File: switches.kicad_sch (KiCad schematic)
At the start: 149 parts, among them SW10 SW_Push, SW11 SW_Push, SW12 SW_Push, SW13 SW_Push, SW14 SW_Push, SW15 SW_Push, SW16 SW_Push, SW17 SW_Push, SW18 SW_Push, SW19 SW_Push, SW20 SW_Push, SW21 SW_Push, SW22 SW_Push, SW23 SW_Push, SW24 SW_Push, SW25 SW_Push, SW26 SW_Push, SW27 SW_Push, SW28 SW_Push, SW29 SW_Push, SW3 SW_Push, SW30 SW_Push, SW31 SW_Push, SW32 SW_Push, SW33 SW_Push, SW34 SW_Push, SW35 SW_Push, SW36 SW_Push, SW37 SW_Push, SW38 SW_Push, SW39 SW_Push, SW4 SW_Push, SW40 SW_Push, SW41 SW_Push, SW42 SW_Push, SW43 SW_Push, SW44 SW_Push, SW45 SW_Push, SW46 SW_Push, SW47 SW_Push, SW48 SW_Push, SW49 SW_Push, SW5 SW_Push, SW50 SW_Push, SW51 SW_Push, SW52 SW_Push, SW53 SW_Push, SW54 SW_Push, SW55 SW_Push, SW56 SW_Push, SW57 SW_Push, SW58 SW_Push, SW59 SW_Push, SW6 SW_Push, SW60 SW_Push, SW61 SW_Push, SW62 SW_Push, SW63 SW_Push, SW64 SW_Push, SW65 SW_Push, SW66 SW_Push, SW67 SW_Push, SW68 SW_Push, SW69 SW_Push, SW7 SW_Push, SW70 SW_Push, SW71 SW_Push, SW72 SW_Push, SW73 SW_Push, SW74 SW_Push, SW75 SW_Push, SW76 SW_Push, SW77 SW_Push, SW78 SW_Push, SW79 SW_Push, SW8 SW_Push, SW80 SW_Push, SW81 SW_Push, SW82 SW_Push, SW83 SW_Push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

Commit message: update footpoint and add pcb layout
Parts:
- SW10, SW11, SW12, SW13, SW14, SW15, SW16, SW17, SW18, SW19, SW20, SW21, SW22, SW23, SW24, SW25, SW26, SW27, SW28, SW29, SW3, SW30, SW31, SW32, SW33, SW34, SW35, SW36, SW37, SW38, SW39, SW4, SW40, SW41, SW42, SW43, SW44, SW45, SW46, SW47, SW48, SW49, SW5, SW50, SW51, SW52, SW53, SW54, SW55, SW56, SW57, SW58, SW59, SW6, SW60, SW61, SW62, SW63, SW64, SW65, SW66, SW67, SW68, SW69, SW7, SW70, SW71, SW72, SW73, SW74, SW75, SW76, SW77, SW78, SW79, SW8, SW80, SW81, SW82, SW83, SW84, SW85, SW86, SW9: footprint keyswitches:Kailh_socket_MX_optional -> keyswitches:Kailh_socket_MX

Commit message: remove key
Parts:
- removed D13, D48: 1N4148, Diode_SMD:D_0603_1608Metric, symbol Diode:1N4148
- removed SW12, SW13, SW17, SW19, SW33, SW34, SW4, SW55, SW57, SW6, SW63, SW64, SW70, SW72, SW77, SW8, SW81, SW83, SW85: SW_Push, keyswitches:Kailh_socket_MX, symbol Switch:SW_Push

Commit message: change pin default and try layout
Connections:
- net col6: no longer SW32.2
- net col7: now also SW32.2

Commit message: modify pcb footprint
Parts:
- D10, D11, D12, D14, D15, D16, D17, D18, D19, D20, D21, D22, D23, D24, D25, D26, D27, D28, D29, D30, D31, D32, D33, D34, D35, D36, D37, D38, D39, D4, D40, D41, D42, D43, D44, D45, D46, D47, D49, D5, D50, D51, D52, D53, D54, D55, D56, D57, D58, D59, D6, D60, D61, D62, D63, D64, D65, D66, D67, D68, D7, D8, D9: value 1N4148 -> (none); footprint Diode_SMD:D_0603_1608Metric -> (none)
- SW10, SW11, SW14, SW15, SW16, SW18, SW20, SW21, SW22, SW23, SW24, SW25, SW26, SW27, SW28, SW29, SW3, SW30, SW31, SW32, SW35, SW36, SW37, SW38, SW39, SW40, SW41, SW42, SW43, SW44, SW45, SW46, SW47, SW48, SW49, SW5, SW50, SW51, SW52, SW53, SW54, SW56, SW58, SW59, SW60, SW61, SW62, SW65, SW66, SW67, SW68, SW69, SW7, SW71, SW73, SW74, SW75, SW76, SW78, SW79, SW80, SW82, SW84, SW86, SW9: value SW_Push -> (none); footprint keyswitches:Kailh_socket_MX -> (none)

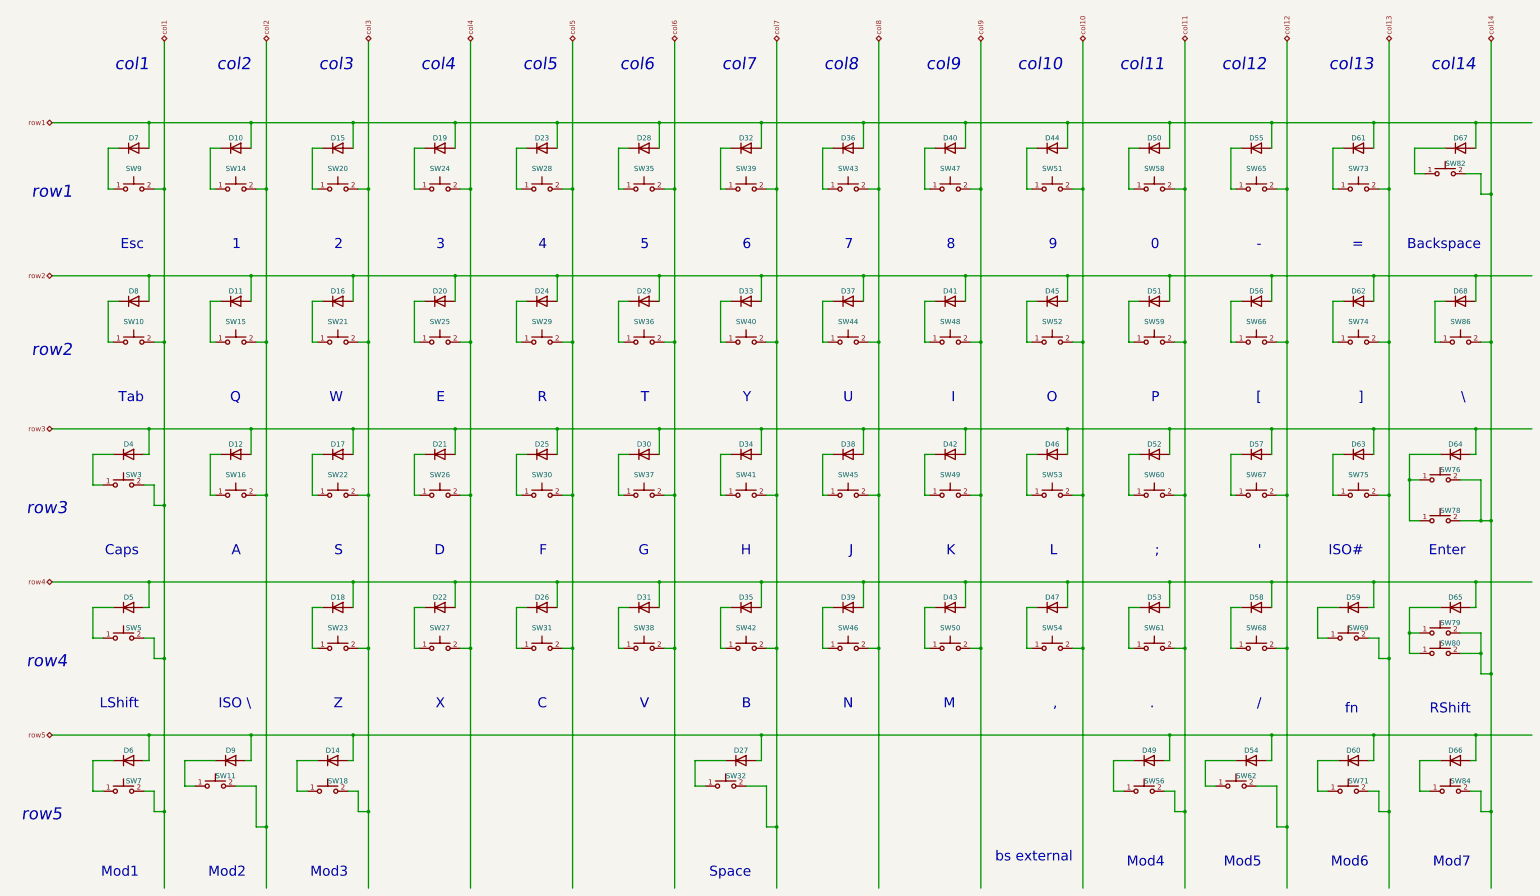
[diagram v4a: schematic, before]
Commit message: change Diode direction and update PR #1 footprint
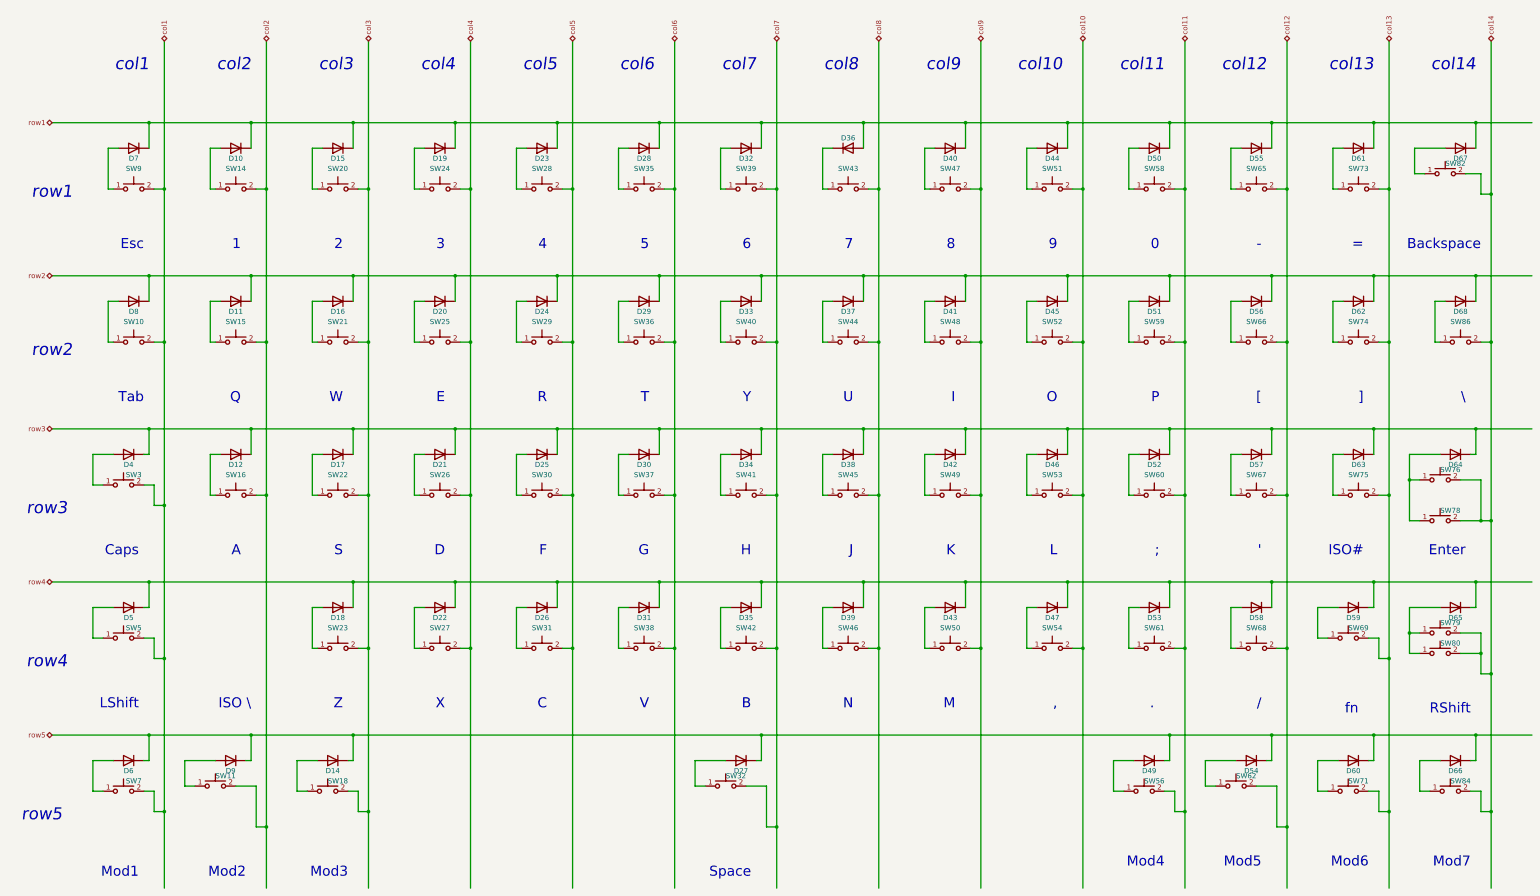
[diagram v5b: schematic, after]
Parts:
- D10, D11, D12, D14, D15, D16, D17, D18, D19, D20, D21, D22, D23, D24, D25, D26, D27, D28, D29, D30, D31, D32, D33, D34, D35, D36, D37, D38, D39, D4, D40, D41, D42, D43, D44, D45, D46, D47, D49, D5, D50, D51, D52, D53, D54, D55, D56, D57, D58, D59, D6, D60, D61, D62, D63, D64, D65, D66, D67, D68, D7, D8, D9: value (none) -> 1N4148; footprint (none) -> Diode_SMD:D_0805_2012Metric
- SW10, SW11, SW14, SW15, SW16, SW18, SW20, SW21, SW22, SW23, SW24, SW25, SW26, SW27, SW28, SW29, SW3, SW30, SW31, SW32, SW35, SW36, SW37, SW38, SW39, SW40, SW41, SW42, SW43, SW44, SW45, SW46, SW47, SW48, SW49, SW5, SW50, SW51, SW52, SW53, SW54, SW56, SW58, SW59, SW60, SW61, SW62, SW65, SW66, SW67, SW68, SW69, SW7, SW71, SW73, SW74, SW75, SW76, SW78, SW79, SW80, SW82, SW84, SW86, SW9: value (none) -> SW_Push; footprint (none) -> keyswitches:Kailh_socket_MX
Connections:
- net row1: now also D10.1 (K), D15.1 (K), D19.1 (K), D23.1 (K), D28.1 (K), D32.1 (K), D40.1 (K), D44.1 (K), D50.1 (K), D55.1 (K), D61.1 (K), D67.1 (K), D7.1 (K); no longer D10.2 (A), D15.2 (A), D19.2 (A), D23.2 (A), D28.2 (A), D32.2 (A), D40.2 (A), D44.2 (A), D50.2 (A), D55.2 (A), D61.2 (A), D67.2 (A), D7.2 (A)
- net row2: now also D11.1 (K), D16.1 (K), D20.1 (K), D24.1 (K), D29.1 (K), D33.1 (K), D37.1 (K), D41.1 (K), D45.1 (K), D51.1 (K), D56.1 (K), D62.1 (K), D68.1 (K), D8.1 (K); no longer D11.2 (A), D16.2 (A), D20.2 (A), D24.2 (A), D29.2 (A), D33.2 (A), D37.2 (A), D41.2 (A), D45.2 (A), D51.2 (A), D56.2 (A), D62.2 (A), D68.2 (A), D8.2 (A)
- net row3: now also D12.1 (K), D17.1 (K), D21.1 (K), D25.1 (K), D30.1 (K), D34.1 (K), D38.1 (K), D4.1 (K), D42.1 (K), D46.1 (K), D52.1 (K), D57.1 (K), D63.1 (K), D64.1 (K); no longer D12.2 (A), D17.2 (A), D21.2 (A), D25.2 (A), D30.2 (A), D34.2 (A), D38.2 (A), D4.2 (A), D42.2 (A), D46.2 (A), D52.2 (A), D57.2 (A), D63.2 (A), D64.2 (A)
- net row4: now also D18.1 (K), D22.1 (K), D26.1 (K), D31.1 (K), D35.1 (K), D39.1 (K), D43.1 (K), D47.1 (K), D5.1 (K), D53.1 (K), D58.1 (K), D59.1 (K), D65.1 (K); no longer D18.2 (A), D22.2 (A), D26.2 (A), D31.2 (A), D35.2 (A), D39.2 (A), D43.2 (A), D47.2 (A), D5.2 (A), D53.2 (A), D58.2 (A), D59.2 (A), D65.2 (A)
- net row5: now also D14.1 (K), D27.1 (K), D49.1 (K), D54.1 (K), D6.1 (K), D60.1 (K), D66.1 (K), D9.1 (K); no longer D14.2 (A), D27.2 (A), D49.2 (A), D54.2 (A), D6.2 (A), D60.2 (A), D66.2 (A), D9.2 (A)
- net at SW7.1: now also D6.2 (A); no longer D6.1 (K)
- net at SW59.1: now also D51.2 (A); no longer D51.1 (K)
- net at SW44.1: now also D37.2 (A); no longer D37.1 (K)
- net at SW28.1: now also D23.2 (A); no longer D23.1 (K)
- net at SW9.1: now also D7.2 (A); no longer D7.1 (K)
- net at SW49.1: now also D42.2 (A); no longer D42.1 (K)
- net at SW66.1: now also D56.2 (A); no longer D56.1 (K)
- net at SW18.1: now also D14.2 (A); no longer D14.1 (K)
- net at SW75.1: now also D63.2 (A); no longer D63.1 (K)
- net at SW40.1: now also D33.2 (A); no longer D33.1 (K)
- net at SW61.1: now also D53.2 (A); no longer D53.1 (K)
- net at SW26.1: now also D21.2 (A); no longer D21.1 (K)
- net at SW45.1: now also D38.2 (A); no longer D38.1 (K)
- net at SW10.1: now also D8.2 (A); no longer D8.1 (K)
- net at SW60.1: now also D52.2 (A); no longer D52.1 (K)
- net at SW62.1: now also D54.2 (A); no longer D54.1 (K)
- net at SW24.1: now also D19.2 (A); no longer D19.1 (K)
- net at SW22.1: now also D17.2 (A); no longer D17.1 (K)
- net at SW86.1: now also D68.2 (A); no longer D68.1 (K)
- net at SW30.1: now also D25.2 (A); no longer D25.1 (K)
- net at SW76.1, SW78.1: now also D64.2 (A); no longer D64.1 (K)
- net at SW51.1: now also D44.2 (A); no longer D44.1 (K)
- net at SW54.1: now also D47.2 (A); no longer D47.1 (K)
- net at SW74.1: now also D62.2 (A); no longer D62.1 (K)
- net at SW36.1: now also D29.2 (A); no longer D29.1 (K)
- net at SW15.1: now also D11.2 (A); no longer D11.1 (K)
- net at SW5.1: now also D5.2 (A); no longer D5.1 (K)
- net at SW31.1: now also D26.2 (A); no longer D26.1 (K)
- net at SW21.1: now also D16.2 (A); no longer D16.1 (K)
- net at SW48.1: now also D41.2 (A); no longer D41.1 (K)
- net at SW47.1: now also D40.2 (A); no longer D40.1 (K)
- net at SW14.1: now also D10.2 (A); no longer D10.1 (K)
- net at SW38.1: now also D31.2 (A); no longer D31.1 (K)
- net at SW23.1: now also D18.2 (A); no longer D18.1 (K)
- net at SW79.1, SW80.1: now also D65.2 (A); no longer D65.1 (K)
- net at SW27.1: now also D22.2 (A); no longer D22.1 (K)
- net at SW41.1: now also D34.2 (A); no longer D34.1 (K)
- net at SW11.1: now also D9.2 (A); no longer D9.1 (K)
- net at SW52.1: now also D45.2 (A); no longer D45.1 (K)
- net at SW53.1: now also D46.2 (A); no longer D46.1 (K)
- net at SW67.1: now also D57.2 (A); no longer D57.1 (K)
- net at SW82.1: now also D67.2 (A); no longer D67.1 (K)
- net at SW3.1: now also D4.2 (A); no longer D4.1 (K)
- net at SW56.1: now also D49.2 (A); no longer D49.1 (K)
- net at SW84.1: now also D66.2 (A); no longer D66.1 (K)
- net at SW71.1: now also D60.2 (A); no longer D60.1 (K)
- net at SW50.1: now also D43.2 (A); no longer D43.1 (K)
- net at SW35.1: now also D28.2 (A); no longer D28.1 (K)
- net at SW20.1: now also D15.2 (A); no longer D15.1 (K)
- net at SW73.1: now also D61.2 (A); no longer D61.1 (K)
- net at SW39.1: now also D32.2 (A); no longer D32.1 (K)
- net at SW16.1: now also D12.2 (A); no longer D12.1 (K)
- net at SW69.1: now also D59.2 (A); no longer D59.1 (K)
- net at SW32.1: now also D27.2 (A); no longer D27.1 (K)
- net at SW37.1: now also D30.2 (A); no longer D30.1 (K)
- net at SW46.1: now also D39.2 (A); no longer D39.1 (K)
- net at SW58.1: now also D50.2 (A); no longer D50.1 (K)
- net at SW65.1: now also D55.2 (A); no longer D55.1 (K)
- net at SW25.1: now also D20.2 (A); no longer D20.1 (K)
- net at SW29.1: now also D24.2 (A); no longer D24.1 (K)
- net at SW42.1: now also D35.2 (A); no longer D35.1 (K)
- net at SW68.1: now also D58.2 (A); no longer D58.1 (K)
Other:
- note removed: "bs external"
- moved on the sheet: D10, D11, D12, D14, D15, D16, D17, D18, D19, D20, D21, D22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

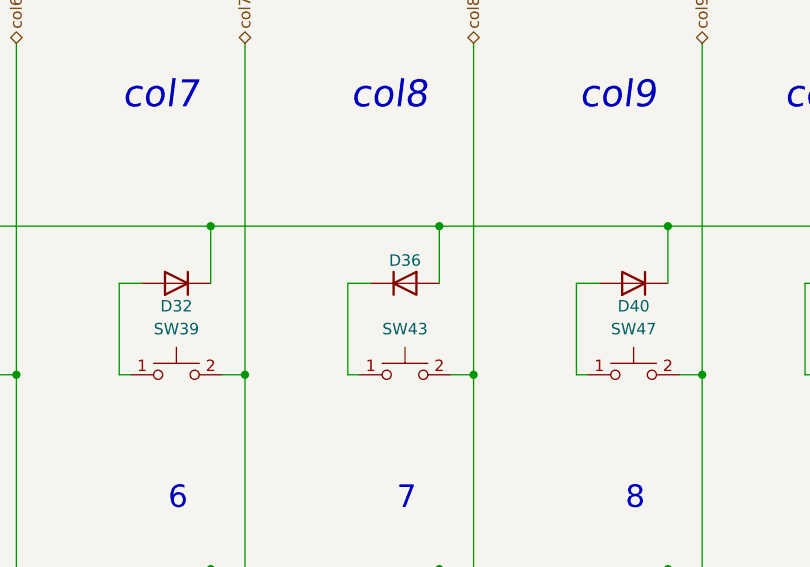
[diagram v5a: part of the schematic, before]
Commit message: fix diode direction on row1
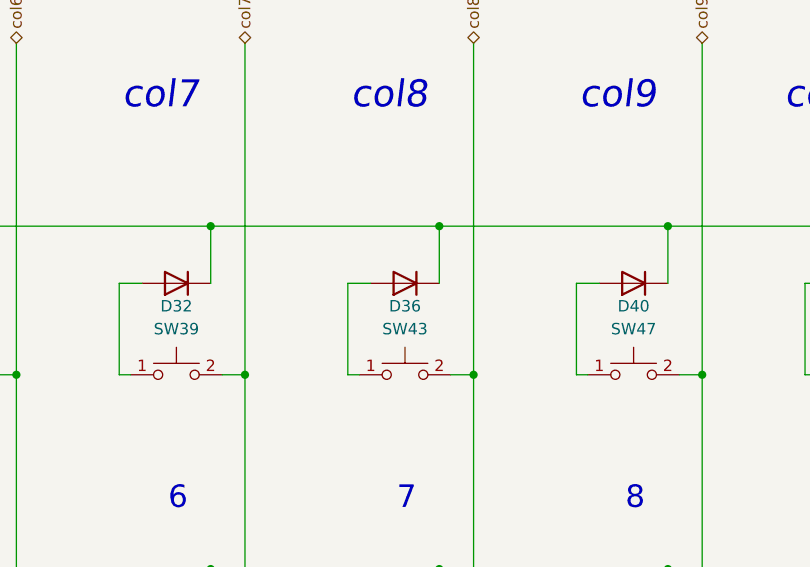
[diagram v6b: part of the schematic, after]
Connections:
- net row1: now also D36.1 (K); no longer D36.2 (A)
- net at SW43.1: now also D36.2 (A); no longer D36.1 (K)
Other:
- moved on the sheet: D36
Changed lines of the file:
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@@
     (pin "2")
   )
-  (symbol (lib_id "Diode:1N4148") (at 223.52 60.96 0) (unit 1)
+  (symbol (lib_id "Diode:1N4148") (at 223.52 60.96 180) (unit 1)
     (in_bom yes) (on_board yes)
-    (property "Reference" "D36" (id 0) (at 223.52 58.42 0))
-    (property "Value" "1N4148" (id 1) (at 223.52 57.15 0)
+    (property "Reference" "D36" (id 0) (at 223.52 63.5 0))
+    (property "Value" "1N4148" (id 1) (at 223.52 64.77 0)
       (effects (font (size 1.27 1.27)) hide)
     )
-    (property "Footprint" "Diode_SMD:D_0805_2012Metric" (id 2) (at 223.52 65.405 0)
+    (property "Footprint" "Diode_SMD:D_0805_2012Metric" (id 2) (at 223.52 56.515 0)
       (effects (font (size 1.27 1.27)) hide)
     )
